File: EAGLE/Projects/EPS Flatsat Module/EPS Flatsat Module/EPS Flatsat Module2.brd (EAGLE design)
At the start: 90.2 x 95.9 mm, 32 parts, among them J1 ESQ-126-39-G-D, J2 ESQ-126-39-G-D, J3 TSW-110-23-F-D, J4 TSW-110-23-F-D, T1 2N3904, T2 2N3904, U1 Value, U2 Value, U3 Value, U4 Value, U5 Value, U6 Value

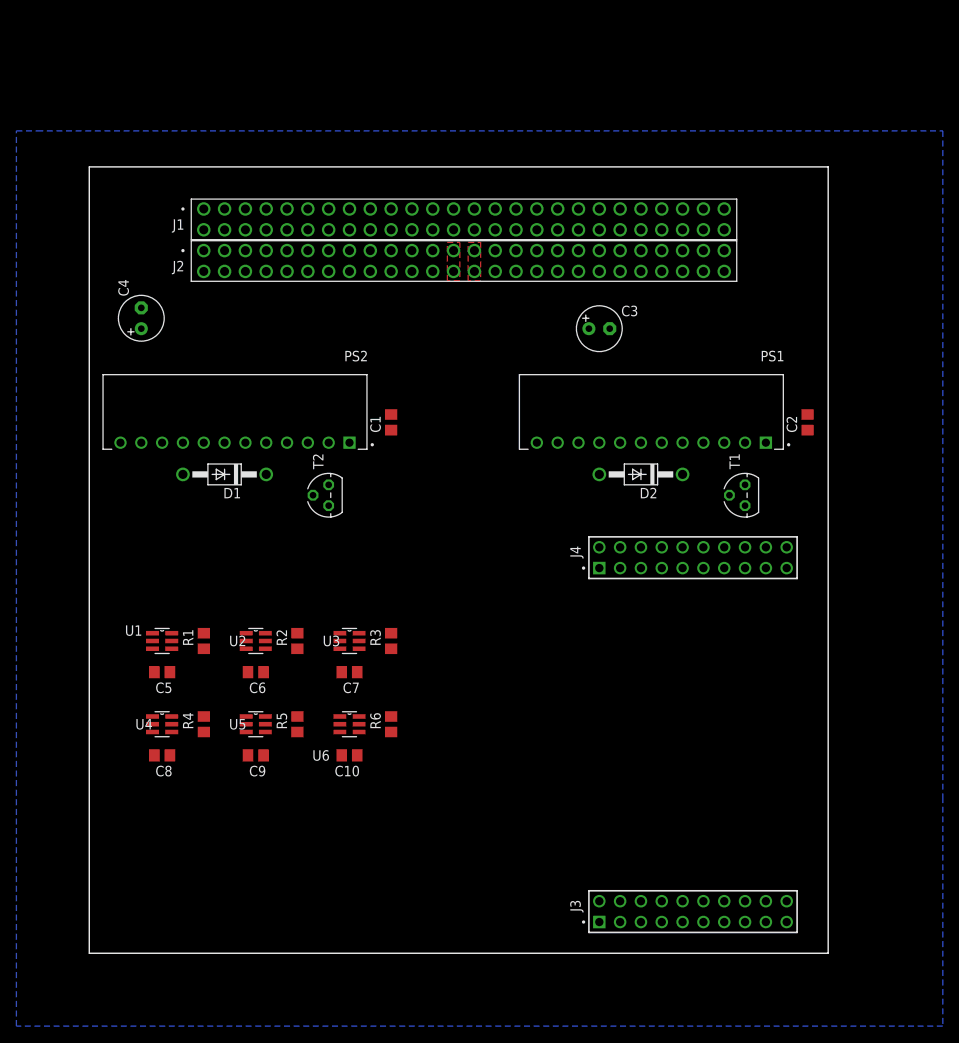
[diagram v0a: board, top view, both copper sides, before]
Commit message: Updated flatsat module schematic/board
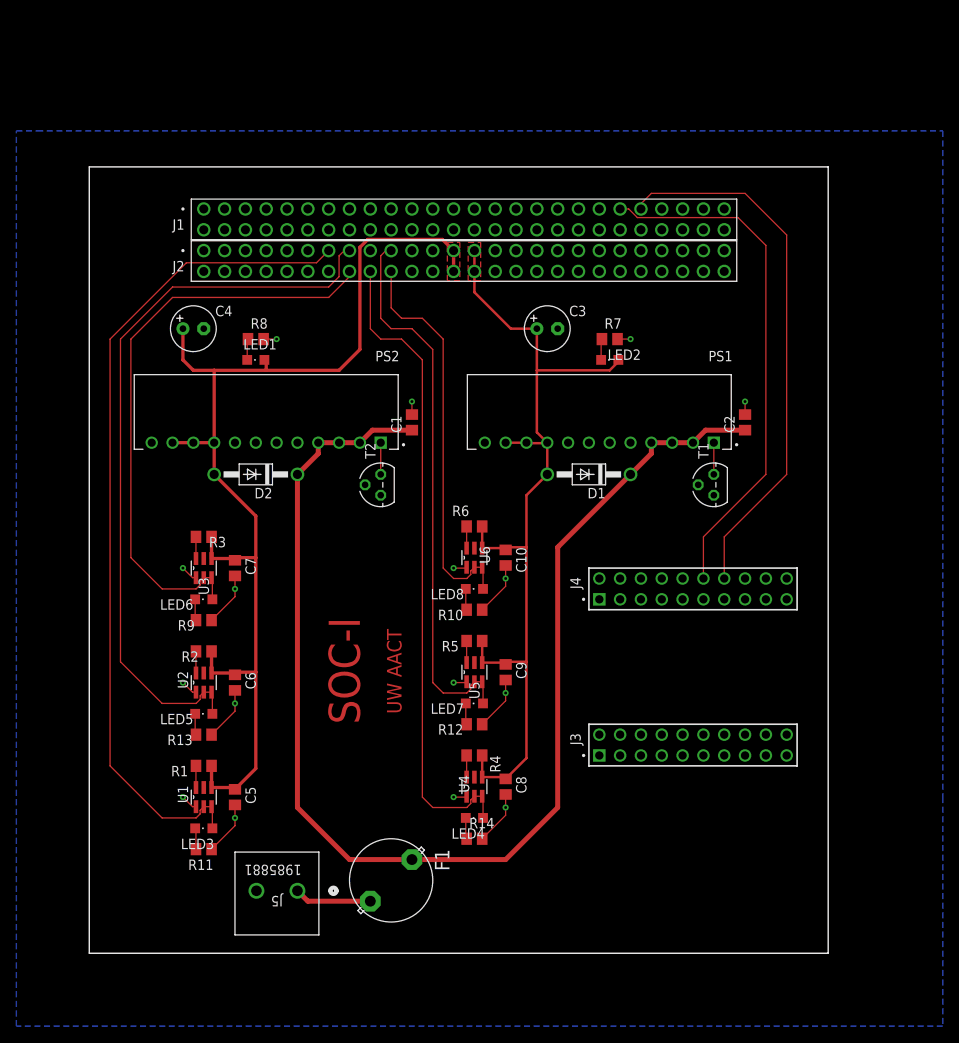
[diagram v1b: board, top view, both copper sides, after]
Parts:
- added F1: (no value), fuse:19559
- added J5: 1985881, 1985881:CONN_1715022_PXC
- added LED1, LED2, LED3, LED4, LED5, LED6, LED7, LED8: (no value), led:CHIPLED_0805
- added R10, R11, R12, R13, R14, R7, R8, R9: (no value), rcl:R0805
- moved D2 47.0 mm to (20.3, 58.4)
- moved D1 44.5 mm to (61.0, 58.4)
- moved C8 42.1 mm to (50.8, 20.3), turned to 270 degrees
- moved U4 38.9 mm to (47.0, 20.3), turned to 90 degrees
- moved R4 33.2 mm to (47.0, 24.1), turned to 180 degrees
- moved C9 32.1 mm to (50.8, 34.3), turned to 270 degrees
- moved C10 30.7 mm to (50.8, 48.3), turned to 270 degrees
- moved U5 27.4 mm to (47.0, 34.3), turned to 90 degrees
- moved R6 26.2 mm to (47.0, 52.1), turned to 180 degrees
- moved R3 26.2 mm to (14.0, 50.8), turned to 180 degrees
- moved U6 25.4 mm to (47.0, 48.3), turned to 90 degrees
- moved R5 23.9 mm to (47.0, 38.1), turned to 180 degrees
- moved J3 20.3 mm to (62.2, 24.1)
- moved U3 19.9 mm to (14.0, 47.0), turned to 90 degrees
- moved U1 19.7 mm to (14.0, 19.1), turned to 90 degrees
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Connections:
- new net N$10: LED2.C, R7.1
- new net N$11: LED6.C, R9.1
- new net N$12: LED3.C, R11.1
- new net N$13: LED4.C, R14.1
- new net N$14: LED7.C, R12.1
- new net N$15: LED5.C, R13.1
- new net N$16: LED8.C, R10.1
- new net N$17: F1.2, J5.1
- new net N$9: LED1.C, R8.1
- net 3V3SYS: now also LED2.A
- net 5VSYS: now also LED1.A
- net GND: now also J5.2, R10.2, R11.2, R12.2, R13.2, R14.2, R7.2, R8.2, R9.2
- net PDM10: now also LED8.A
- net PDM5: now also LED3.A
- net PDM6: now also LED5.A
- net PDM7: now also LED6.A
- net PDM8: now also LED4.A
- net PDM9: now also LED7.A
- net VIN: now also F1.1
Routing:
- net VIN: track 0.00 -> 155.9 mm
- net 5VSYS: track 0.00 -> 137.2 mm
- net 3V3SYS: track 0.00 -> 110.8 mm
- net PDM5: track 0.00 -> 101.7 mm
- net PDM6: track 0.00 -> 90.0 mm
- net PDM8: track 0.00 -> 79.6 mm
- net PDM7: track 0.00 -> 72.1 mm
- net PDM9: track 0.00 -> 67.8 mm
- net SCL: track 0.00 -> 66.1 mm
- net SDA: track 0.00 -> 63.4 mm
- net GND: track 0.00 -> 57.0 mm, vias 0 -> 16
- net PDM10: track 0.00 -> 49.1 mm
- net N$17: track 0.00 -> 9.42 mm
- net N$2: track 0.00 -> 3.87 mm
- net N$1: track 0.00 -> 3.87 mm
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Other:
- board text added: "SOC-I"
- board text added: "UW AACT"

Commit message: Updated fuse, changed MSP header spacing, small layout edits
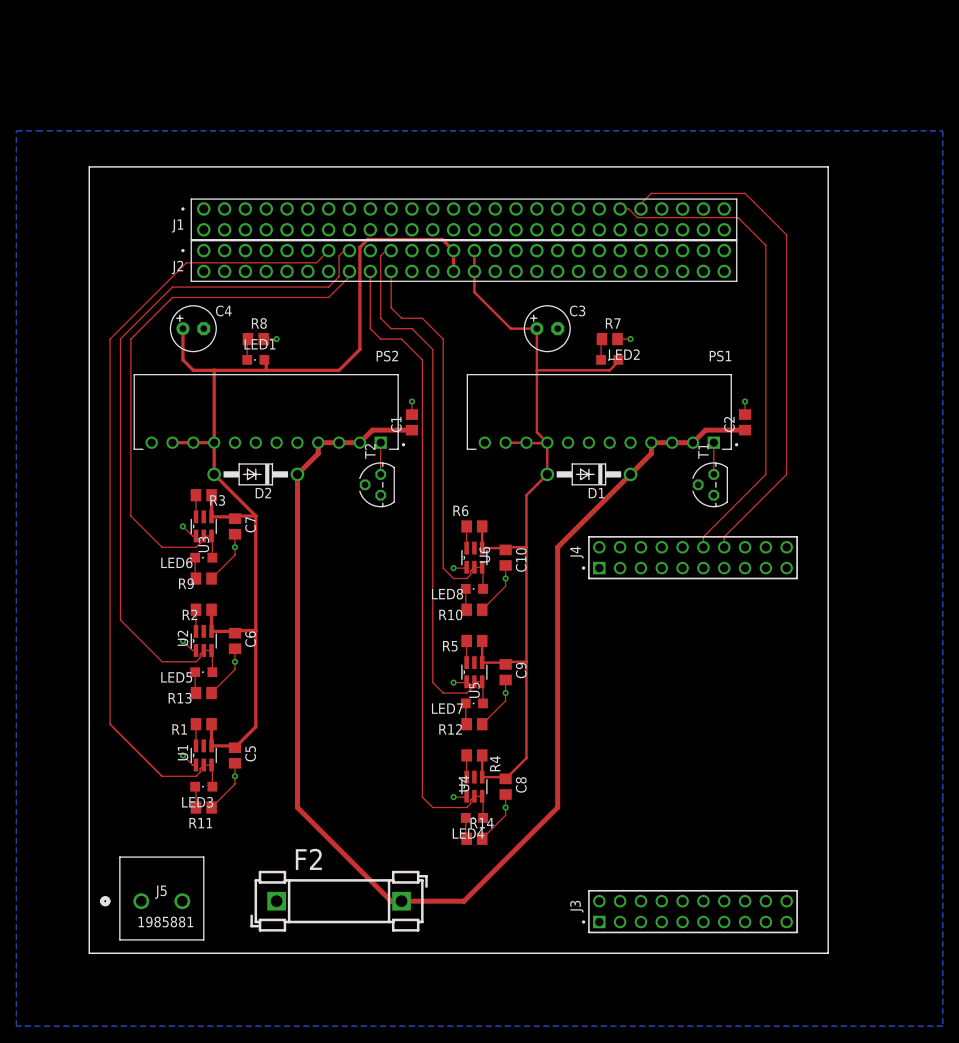
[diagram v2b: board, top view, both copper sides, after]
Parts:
- removed F1: (no value), fuse:19559
- added F2: FUSEBLANK_5X20MM, fuse:FUSE_HOLDER_5X20MM
- moved J3 20.3 mm to (62.2, 3.81)
- moved J5 19.1 mm to (6.35, 6.35), turned to 0 degrees
- moved R3 5.08 mm to (14.0, 55.9)
- moved R1 5.08 mm to (14.0, 27.9)
- moved R11 5.08 mm to (14.0, 17.8)
- moved LED3 5.08 mm to (14.0, 20.3)
- moved C5 5.08 mm to (17.8, 24.1)
- moved C6 5.08 mm to (17.8, 38.1)
- moved C7 5.08 mm to (17.8, 52.1)
- moved LED5 5.08 mm to (14.0, 34.3)
- moved LED6 5.08 mm to (14.0, 48.3)
- moved R13 5.08 mm to (14.0, 31.8)
- moved R2 5.08 mm to (14.0, 41.9)
- moved R9 5.08 mm to (14.0, 45.7)
- moved U1 5.08 mm to (14.0, 24.1)
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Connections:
- new net MSP_3V3: J3.01
- new net MSP_5V: J3.02
- net GND: now also J5.1; no longer J5.2
- net N$17: now also F2.1, J5.2; no longer F1.2, J5.1
- net VIN: now also F2.2; no longer F1.1
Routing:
- net N$17: track 9.42 -> 0.00 mm
- net 5VSYS: track 137.2 -> 132.1 mm
- net PDM6: track 90.0 -> 84.9 mm
- net PDM5: track 101.7 -> 96.7 mm
- net PDM7: track 72.1 -> 67.0 mm
- net VIN: track 155.9 -> 160.2 mm
- net SDA: track 63.4 -> 59.6 mm
- net SCL: track 66.1 -> 62.3 mm
- removed copper zone on layer 1, net 3V3SYS
- removed copper zone on layer 1, net 5VSYS
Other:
- board text added: "MSP 430"

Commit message: Added TVS diode, changed microcontroller to Arduino Nano, redid traces
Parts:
- removed J3, J4: TSW-110-23-F-D, TSW-110-23-F-D:SAMTEC_TSW-110-23-F-D
- added D3: ZPY, diode:DO41Z10
- added JP2, JP3: -, Arduino-connectors:1X15-CASTELL
- moved J1 5.08 mm to (14.0, 85.7)
- moved J2 5.08 mm to (14.0, 90.8)
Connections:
- removed net MSP_3V3: J3.01
- removed net MSP_5V: J3.02
- new net N$19: J2.51
- net 3V3ONOFF: now also JP3.15
- net 5VONOFF: now also JP3.14
- net GND: now also D3.A, JP2.14; no longer J3.04, J4.02
- net PDM10EN: now also JP3.8
- net PDM5EN: now also JP3.13
- net PDM6EN: now also JP3.12
- net PDM7EN: now also JP3.11
- net PDM8EN: now also JP3.10
- net PDM9EN: now also JP3.9
- net SCL: now also JP2.9; no longer J4.14
- net SDA: now also JP2.8; no longer J4.12
- net VIN: now also D3.C, JP2.15
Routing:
- net GND: track 57.0 -> 548.5 mm, vias 16 -> 5
- net PDM6EN: track 0.00 -> 128.6 mm
- net PDM7EN: track 0.00 -> 102.4 mm, vias 0 -> 4
- net PDM8EN: track 0.00 -> 92.5 mm, vias 0 -> 2
- net 5VONOFF: track 0.00 -> 91.9 mm
- net PDM5EN: track 0.00 -> 78.1 mm
- net VIN: track 160.2 -> 227.9 mm, vias 0 -> 2
- net PDM9EN: track 0.00 -> 67.3 mm, vias 0 -> 2
- net 3V3ONOFF: track 0.00 -> 61.5 mm
- net PDM10EN: track 0.00 -> 46.3 mm
- net SDA: track 59.6 -> 79.6 mm
- net PDM10: track 49.1 -> 64.8 mm, vias 0 -> 4
- net SCL: track 62.3 -> 76.9 mm
- net N$17: track 0.00 -> 11.5 mm
- net PDM6: track 84.9 -> 94.8 mm, vias 0 -> 2
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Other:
- board text added: "Arduino Nano"
- board text removed: "MSP 430"

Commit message: Update to board layout
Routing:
- net 5VSYS: track 130.1 -> 128.8 mm
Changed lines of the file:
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@@
 <wire x1="14.92" y1="25.2984" x2="17.5616" y2="25.2984" width="0.508" layer="1"/>
 <wire x1="17.5616" y1="25.2984" x2="17.78" y2="25.08" width="0.2032" layer="1"/>
-<wire x1="14.859" y1="29.21" x2="14.859" y2="28.001" width="0.508" layer="1"/>
-<wire x1="14.859" y1="28.001" x2="14.92" y2="27.94" width="0.2032" layer="1"/>
-<wire x1="14.859" y1="29.21" x2="19.685" y2="34.036" width="0.508" layer="1"/>
-<wire x1="19.685" y1="34.036" x2="19.685" y2="38.735" width="0.508" layer="1"/>
+<wire x1="14.8895" y1="27.9705" x2="14.92" y2="27.94" width="0.2032" layer="1"/>
+<wire x1="19.685" y1="32.766" x2="14.8895" y2="27.9705" width="0.508" layer="1"/>
 <wire x1="19.685" y1="38.735" x2="19.304" y2="39.116" width="0.2032" layer="1"/>
 <wire x1="19.304" y1="39.116" x2="17.846" y2="39.116" width="0.508" layer="1"/>
@@
 <wire x1="19.685" y1="25.4" x2="19.685" y2="28.575" width="0.508" layer="16"/>
 <via x="19.685" y="28.575" extent="1-16" drill="0.35"/>
-<wire x1="19.685" y1="28.575" x2="19.685" y2="34.036" width="0.508" layer="1"/>
 <wire x1="15.24" y1="58.42" x2="15.24" y2="62.29" width="0.508" layer="1"/>
 <wire x1="15.24" y1="62.29" x2="15.24" y2="64.77" width="0.508" layer="1"/>
@@
 <wire x1="15.24" y1="62.29" x2="12.7" y2="62.29" width="0.508" layer="1"/>
 <wire x1="12.7" y1="62.29" x2="10.16" y2="62.29" width="0.508" layer="1"/>
+<wire x1="19.685" y1="28.575" x2="19.685" y2="32.766" width="0.508" layer="1"/>
+<wire x1="19.685" y1="38.735" x2="19.685" y2="32.766" width="0.508" layer="1"/>
 </signal>
 <signal name="GND" class="1">

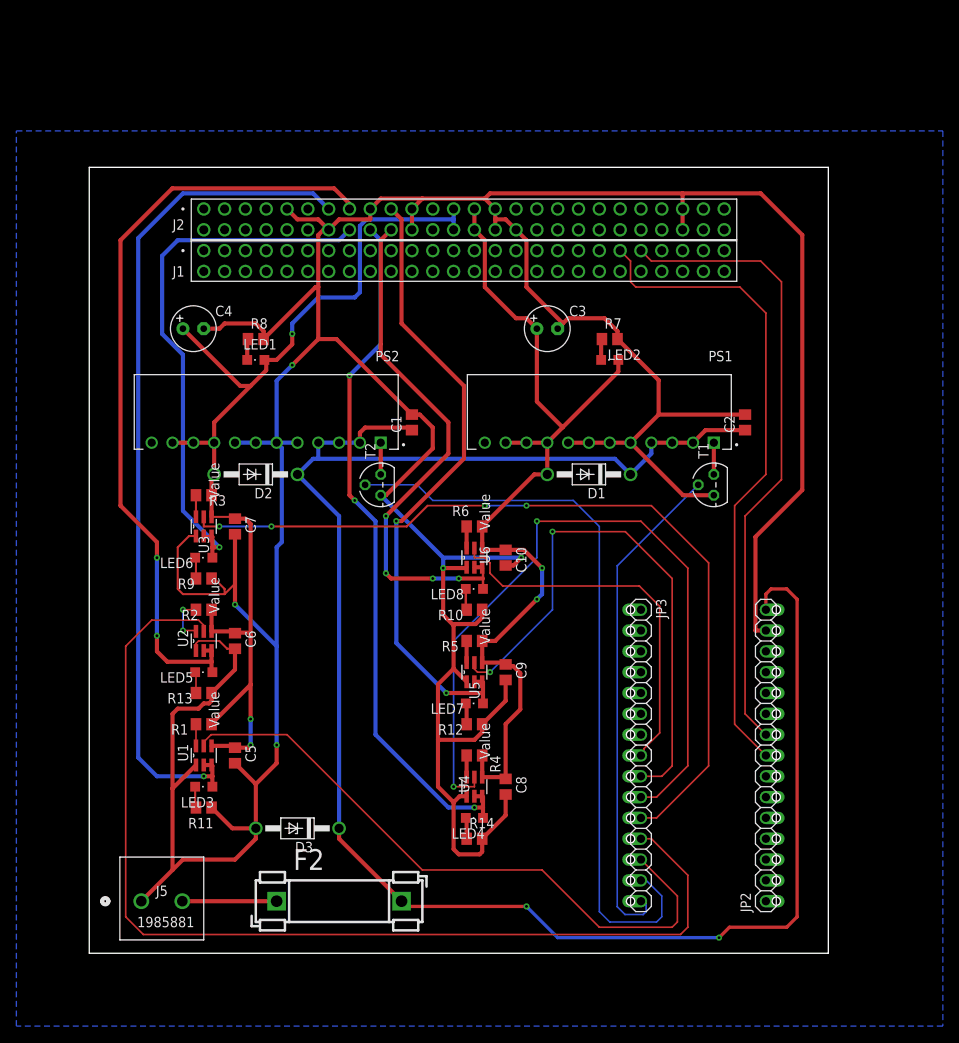
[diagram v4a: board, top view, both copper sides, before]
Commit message: Added current sensing
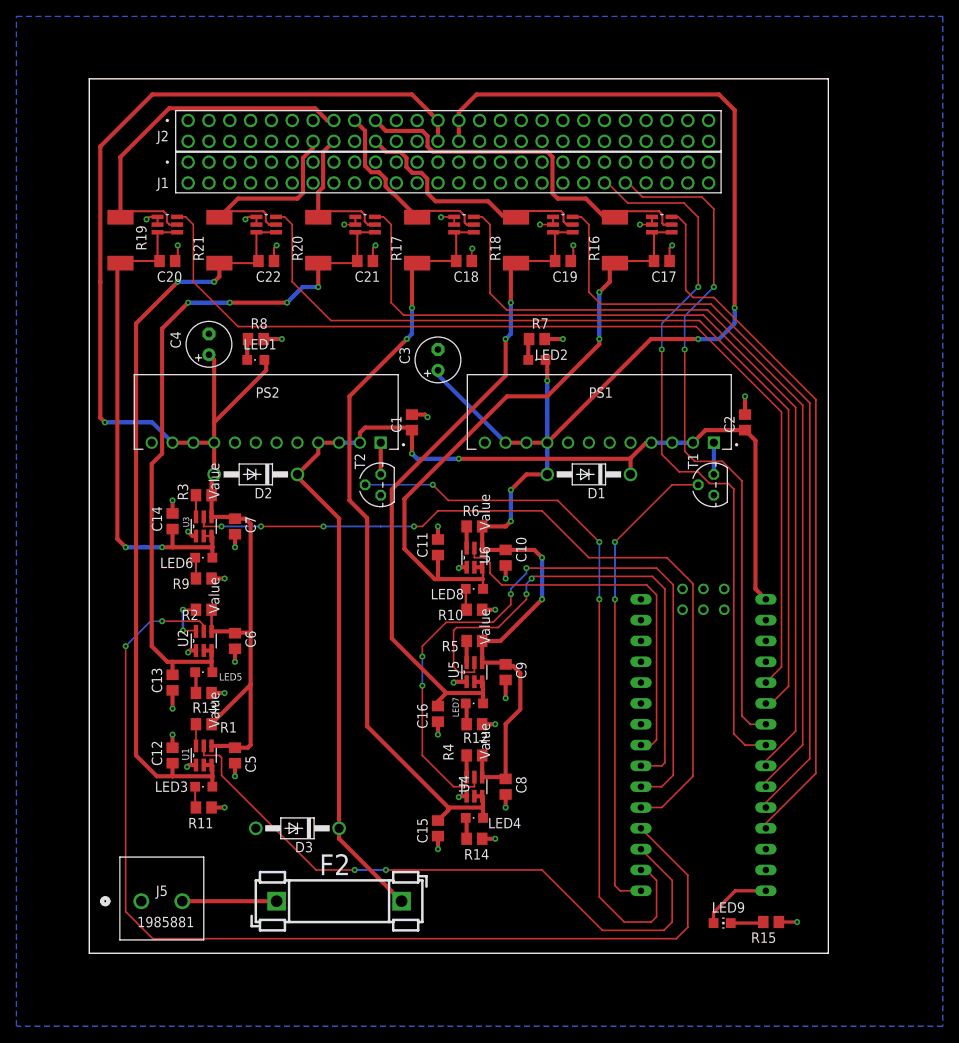
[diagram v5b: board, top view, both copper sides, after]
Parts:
- removed JP2, JP3: -, Arduino-connectors:1X15-CASTELL
- added C11, C12, C13, C14, C15, C16: 0.1u, rcl:C0805
- added C17, C18, C19, C20, C21, C22: 0.1uF, rcl:C0805
- added LED9: (no value), led:CHIP-LED0805
- added R15: (no value), rcl:R0805
- added R16, R17, R18, R19, R20, R21: 0.01, rcl:R2512
- added U$1: NANO, Arduino-clone:NANO
- added U10, U11, U12, U7, U8, U9: ADM4073HWRJZ-REEL7, ADM4073HWRJZ-REEL7:SOT95P290X145-6N
- moved C3 13.9 mm to (42.5, 72.4), turned to 90 degrees
- moved J1 11.0 mm to (12.1, 96.5)
- moved J2 11.0 mm to (12.1, 101.6)
- moved LED2 8.89 mm to (54.6, 72.4)
- moved R7 8.89 mm to (54.6, 74.9)
- moved C4 2.69 mm to (14.6, 74.3), turned to 90 degrees
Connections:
- removed net N$19: J2.51
- removed net PDM10: J2.20, LED8.A, U6.2, U6.3
- removed net PDM10EN: JP3.8, U6.5
- removed net PDM7: J2.16, LED6.A, U3.2, U3.3
- removed net PDM7EN: JP3.11, U3.5
- removed net PDM8: J2.18, LED4.A, U4.2, U4.3
- removed net PDM8EN: JP3.10, U4.5
- removed net PDM9: J2.19, LED7.A, U5.2, U5.3
- removed net PDM9EN: JP3.9, U5.5
- new net ADC0: U$1.A3, U11.6
- new net ADC1: U$1.A2, U7.6
- new net ADC2: U$1.A1, U9.6
- new net ADC3: U$1.A0, U8.6
- new net ADC4: U$1.A6, U12.6
- new net ADC5: U$1.A7, U10.6
- new net N$18: LED9.A, U$1.D13
- new net N$27: LED9.C, R15.2
- new net PDM1: C15.1, C18.1, LED4.A, R17.1, U4.2, U4.3, U7.3, U7.4
- new net PDM1EN: U$1.D7, U4.5
- new net PDM1_OUT: J2.17, R17.2, U7.5
- new net PDM2: C11.1, C17.1, LED8.A, R16.1, U6.2, U6.3, U8.3, U8.4
- new net PDM2EN: U$1.D5, U6.5
- new net PDM2_OUT: J2.19, R16.2, U8.5
- new net PDM3: C16.1, C19.1, LED7.A, R18.1, U5.2, U5.3, U9.3, U9.4
- new net PDM3EN: U$1.D6, U5.5
- new net PDM3_OUT: J2.20, R18.2, U9.5
- new net PDM4: C14.1, C20.1, LED6.A, R19.1, U10.3, U10.4, U3.2, U3.3
- new net PDM4EN: U$1.D8, U3.5
- new net PDM4_OUT: J2.15, R19.2, U10.5
- new net PDM5_OUT: J2.16, R20.2, U11.5
- new net PDM6_OUT: J2.14, R21.2, U12.5
- net 3V3ONOFF: now also U$1.D12; no longer JP3.15
- net 5VONOFF: now also U$1.D11; no longer JP3.14
- net GND: now also C11.2, C12.2, C13.2, C14.2, C15.2, C16.2, C17.2, C18.2, C19.2, C20.2, C21.2, C22.2, J2.10, J2.13, J2.18, J2.31, J2.51, R15.1, U$1.GND, U10.1, U10.2, U11.1, U11.2, U12.1, U12.2, U7.1, U7.2, U8.1, U8.2, U9.1, U9.2; no longer J2.14, J2.17, J2.32, J2.9, JP2.14
- net PDM5: now also C13.1, C21.1, LED5.A, R20.1, U11.3, U11.4, U2.2, U2.3; no longer J2.13, LED3.A, U1.2, U1.3
- net PDM5EN: now also U$1.D9, U2.5; no longer JP3.13, U1.5
- net PDM6: now also C12.1, C22.1, LED3.A, R21.1, U1.2, U1.3, U12.3, U12.4; no longer J2.15, LED5.A, U2.2, U2.3
- net PDM6EN: now also U$1.D10, U1.5; no longer JP3.12, U2.5
- net SCL: now also J1.44, U$1.A5; no longer J1.43, JP2.9
- net SDA: now also J1.42, U$1.A4; no longer J1.41, JP2.8
- net VIN: now also U$1.RAW; no longer JP2.15
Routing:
- net GND: track 548.5 -> 74.4 mm, vias 5 -> 41
- net ADC5: track 0.00 -> 121.5 mm
- net ADC4: track 0.00 -> 113.7 mm
- net ADC0: track 0.00 -> 111.8 mm
- net ADC1: track 0.00 -> 103.0 mm
- net PDM7EN: track 102.4 -> 0.00 mm, vias 4 -> 0
- net PDM4EN: track 0.00 -> 96.8 mm, vias 0 -> 4
- net PDM1: track 0.00 -> 95.7 mm, vias 0 -> 2
- net ADC2: track 0.00 -> 94.8 mm
- net PDM8EN: track 92.5 -> 0.00 mm, vias 2 -> 0
- net PDM1EN: track 0.00 -> 87.1 mm, vias 0 -> 4
- net ADC3: track 0.00 -> 86.4 mm
- net PDM8: track 85.4 -> 0.00 mm, vias 3 -> 0
- net VIN: track 227.9 -> 144.2 mm
- net PDM3: track 0.00 -> 82.7 mm, vias 0 -> 2
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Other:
- board size 90.2 x 95.9 mm -> 90.2 x 106.7 mm
